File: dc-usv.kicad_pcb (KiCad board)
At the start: 4 copper layers, 160 x 100 mm, 310 parts, among them J1 Output 2.0mm, J2 Output 2.0mm, J3 Output 2.0mm, J5 HanRun_HR911105A, J6 USB_C_Receptacle_USB2.0, J7 Input 2.0mm, J8 Input 2.5mm, J9 USB_C_Receptacle_USB2.0, Q1 AON7544, Q10 AO4407A, Q11 2N7002, Q12 MMBT3904, Q13 2N7002, Q14 2N7002, Q15 2N7002, Q16 2N7002, Q17 2N7002, Q18 MMBT3904, Q19 AO4407A, Q2 AO3401A, Q20 2N7002, Q21 AO4407A, Q22 2N7002, Q23 AO4407A, Q24 2N7002, Q25 AO3401A, Q28 MMBT3904, Q29 MMBT3904, Q3 AON7544, Q30 MMBT3904, Q31 2N7002, Q32 AO4407A, Q33 MMBT3904, Q34 2N7002, Q35 AO4407A, Q36 MMBT3904, Q37 2N7002, Q38 AO4407A, Q4 AON7544, Q5 AON7544, Q6 CSD17308Q3, Q7 CSD17308Q3, Q8 AO4407A, Q9 2N7002, SW1 SW_DIP_x02, U1 BQ40z50-R2, U10 LAN8720A, U11 74HC595, U12 SY8105, U13 LM75B, U14 INA219AxD, U15 INA219AxD, U16 CH340G, U17 N066-6448TSWEG03-H28, U2 LM75B, U3 BQ24715, U4 TPS61178x, U5 INA219AxD, U6 INA219AxD, U7 LM75B, U8 SY8120B1ABC, U9 ESP32-WROOM-32E, Y1 12MHz

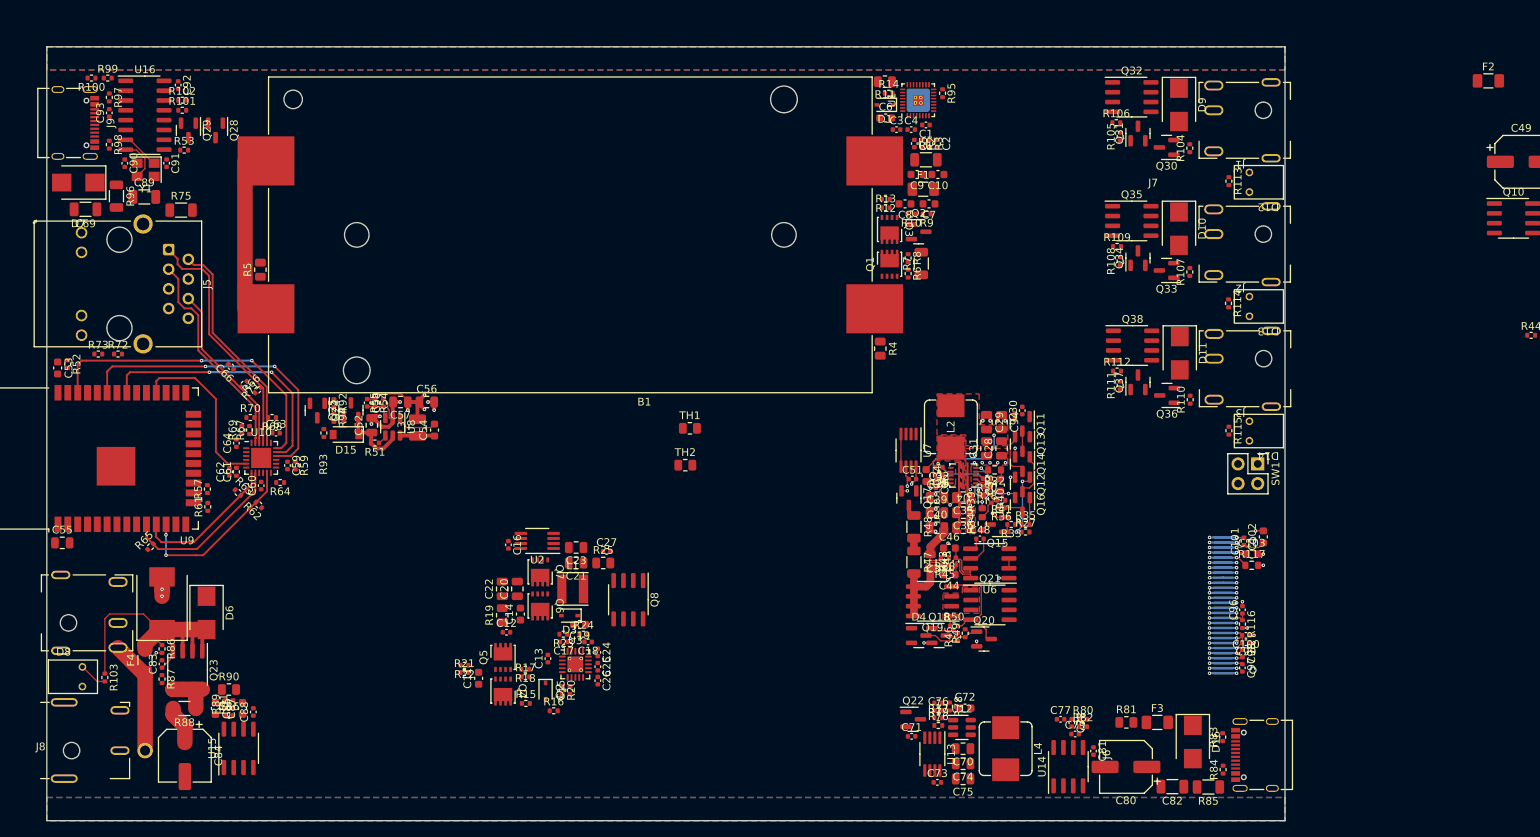
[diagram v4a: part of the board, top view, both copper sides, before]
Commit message: Plan front panel element positioning
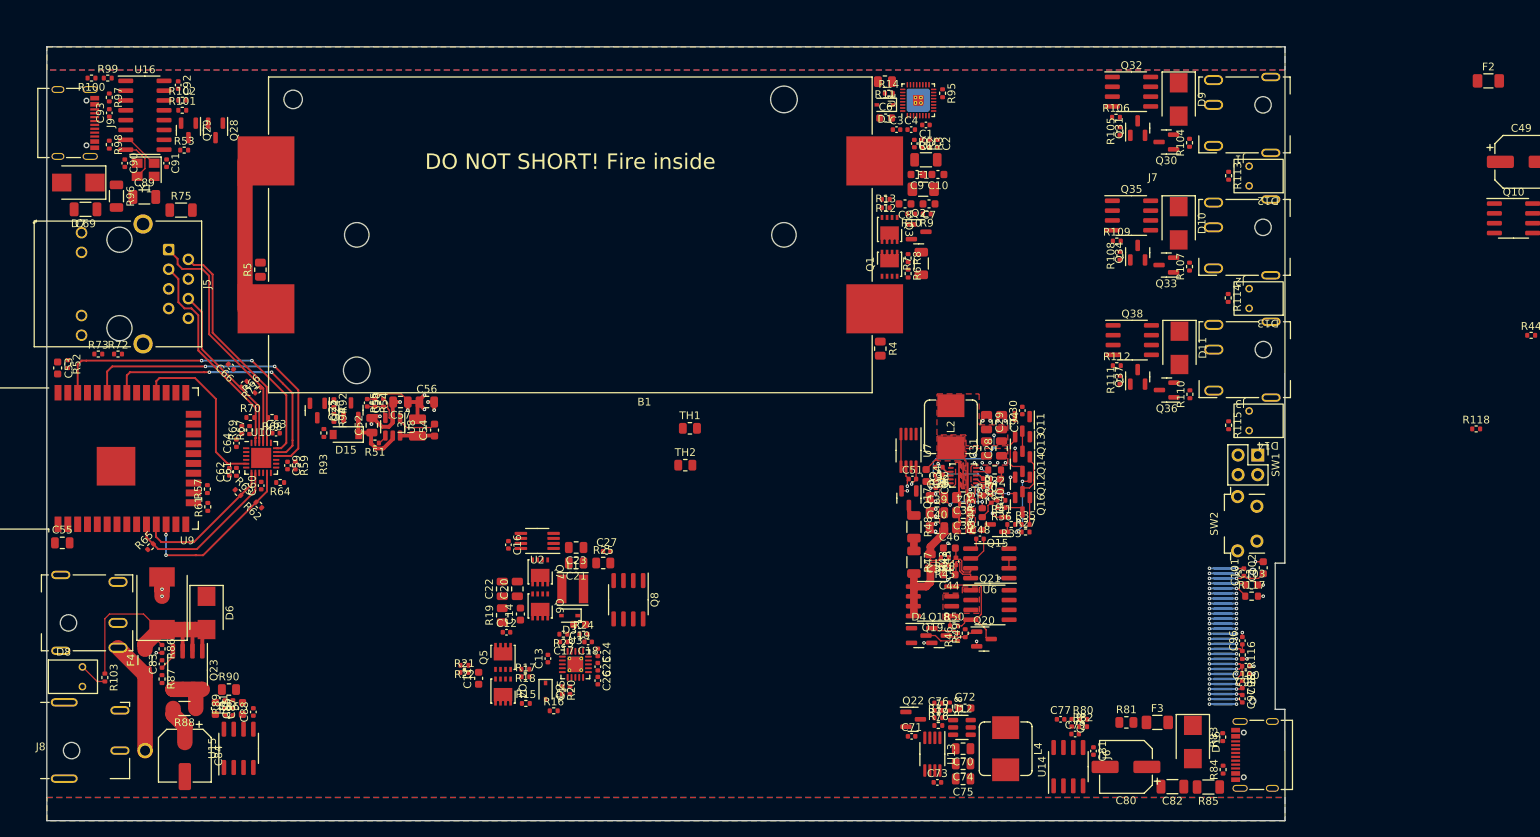
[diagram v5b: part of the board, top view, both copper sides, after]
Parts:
- added R118: 10k, Resistor_SMD:R_0402_1005Metric, F.Cu at (204.7, 69.4)
- added SW2: SW_Push, Button_Switch_SMD_LCSC:x-1825027-x, F.Cu at (176.4, 81.6)
- moved C100 3.99 mm to (174.9, 100.0)
- moved C103 3.99 mm to (175.7, 89.5)
- moved R116 3.99 mm to (174.5, 98.6)
- moved U17 3.99 mm to (173.8, 96.2)
- moved C101 3.99 mm to (174.7, 87.9)
- moved C102 3.99 mm to (177.2, 87.3)
- moved C96 3.99 mm to (174.5, 96.7)
- moved C97 3.99 mm to (174.5, 104.2)
- moved C98 3.99 mm to (174.5, 102.4)
- moved C99 3.99 mm to (174.9, 101.0)
- moved R117 3.99 mm to (175.7, 91.0)
- moved D14 1.33 mm to (179.8, 68.3)
- moved J3 1.18 mm to (181.2, 59.1)
- moved SW1 1.15 mm to (176.5, 72.8)
- moved D13 1.03 mm to (179.8, 52.5)
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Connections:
- U9 pad 5: unconnected-(U9-Pad5) -> /Control Logic/BUTTON
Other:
- outline, holes or cut-outs redrawn
- board text added: "DO NOT SHORT! Fire inside"

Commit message: Partial layout
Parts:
- added C104: 22nF, Capacitor_SMD:C_0402_1005Metric, F.Cu at (46.7, 104.3)
- added CASE1: 1455L1601, Case:1455L1601, F.Cu at (20.0, 20.0)
- added D17: YEL, LED_SMD:LED_0603_1608Metric, F.Cu at (50.3, 104.0)
- added D18: RED, LED_SMD:LED_0603_1608Metric, F.Cu at (50.3, 102.5)
- added D19: GRN, LED_SMD:LED_0603_1608Metric, F.Cu at (50.3, 105.6)
- added Q26: 2N7002, Package_TO_SOT_SMD:SOT-23, F.Cu at (54.2, 108.9)
- added R119: 10k, Resistor_SMD:R_0402_1005Metric, F.Cu at (48.3, 103.5)
- added R120: 5.1k, Resistor_SMD:R_0402_1005Metric, F.Cu at (52.8, 99.3)
- added R121: 10k, Resistor_SMD:R_0402_1005Metric, F.Cu at (48.3, 105.7)
- added U18: SRV05-4, Package_TO_SOT_SMD:SOT-23-6, F.Cu at (29.8, 29.9)
- TH1, TH2: footprint Resistor_SMD:R_0805_2012Metric -> Resistor_SMD:R_0402_1005Metric
- moved R56 136.3 mm to (134.9, 94.2)
- moved R31 130.0 mm to (112.2, 85.0)
- moved R95 99.6 mm to (92.3, 115.6), turned to 180 degrees
- moved C2 96.1 mm to (85.8, 115.0), turned to 180 degrees
- moved U1 95.0 mm to (91.4, 112.5), turned to 0 degrees
- moved C1 94.9 mm to (88.2, 113.5), turned to 90 degrees
- moved C10 94.9 mm to (81.8, 115.0), turned to 90 degrees
- moved R3 94.7 mm to (85.8, 114.0), turned to 180 degrees
- moved R2 93.3 mm to (85.8, 113.0), turned to 180 degrees
- moved R1 93.3 mm to (83.7, 113.5), turned to -90 degrees
- moved C7 92.5 mm to (78.0, 113.9), turned to 90 degrees
- moved C4 92.1 mm to (87.5, 111.6), turned to -90 degrees
- moved C5 92.0 mm to (85.8, 112.0), turned to 180 degrees
- moved F1 91.8 mm to (79.9, 113.1), turned to -90 degrees
- moved R9 91.8 mm to (76.7, 113.6), turned to 90 degrees
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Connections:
- net /Control Logic/ESP32 Debug/VBUS renamed VBUS
- net Net-(B1-Pad1) renamed /Battery Pack/B+
- net Net-(C11-Pad2) renamed /Charger/INFETCOM
- net Net-(C19-Pad2) renamed /Charger/LX
- net Net-(C72-Pad1) renamed /USB Output/LX
- net Net-(C74-Pad1) renamed /USB Output/VOUT
- net Net-(C8-Pad2) renamed /Battery Pack/VBAT
- net Net-(F3-Pad2) renamed /USB Output/VBUS
- net Net-(Q1-Pad5) renamed /Battery Pack/VCOM
- net Net-(Q23-Pad5) renamed /DC Input/DCSMOOTH
- C12 pad 2: /Charger/ACS- -> /Charger/ACS+
- C13 pad 1: /Charger/ACS- -> /Charger/ACS+
- C13 pad 2: /Charger/ACS+ -> /Charger/ACS-
- C14 pad 2: /Charger/ACS+ -> /Charger/ACS-
- C20 pad 1: /Charger/ACS+ -> /Charger/ACS-
- C22 pad 1: /Charger/ACS+ -> /Charger/ACS-
- C66 pad 1: +3.3V -> +3V3
- J5 pad 4: +3.3V -> +3V3
- J5 pad 5: +3.3V -> +3V3
- Q5 pad 5: /Charger/ACS- -> /Charger/ACS+
- Q5 pad 6: /Charger/ACS- -> /Charger/ACS+
- Q5 pad 7: /Charger/ACS- -> /Charger/ACS+
- Q5 pad 8: /Charger/ACS- -> /Charger/ACS+
- Q5 pad 9: /Charger/ACS- -> /Charger/ACS+
- Q6 pad 5: /Charger/ACS+ -> /Charger/ACS-
- Q6 pad 6: /Charger/ACS+ -> /Charger/ACS-
- Q6 pad 7: /Charger/ACS+ -> /Charger/ACS-
- Q6 pad 8: /Charger/ACS+ -> /Charger/ACS-
- Q6 pad 9: /Charger/ACS+ -> /Charger/ACS-
- R19 pad 1: /Charger/ACS- -> /Charger/ACS+
- R19 pad 2: /Charger/ACS+ -> /Charger/ACS-
- R66 pad 1: +3.3V -> +3V3
- R68 pad 1: +3.3V -> +3V3
- R70 pad 1: +3.3V -> +3V3
- R71 pad 1: +3.3V -> +3V3
- U3 pad 1: /Charger/ACS+ -> /Charger/ACS-
- U3 pad 2: /Charger/ACS- -> /Charger/ACS+
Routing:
- net SMBC: track 0.00 -> 222.1 mm, vias 0 -> 12
- net SMBD: track 1.26 -> 221.8 mm, vias 0 -> 12
- net SDA: track 7.65 -> 172.1 mm, vias 4 -> 12
- net SCL: track 3.50 -> 154.0 mm, vias 2 -> 10
- net VSEL1: track 0.93 -> 133.7 mm, vias 0 -> 4
- net GND: track 135.9 -> 266.8 mm, vias 77 -> 197
- net /Control Logic/~{OLED_RST}: track 5.22 -> 135.1 mm, vias 2 -> 5
- net /Control Logic/BUTTON: track 0.00 -> 118.6 mm, vias 0 -> 2
- net DCOK: track 0.00 -> 108.4 mm, vias 0 -> 5
- net /Charger/CS+: track 0.00 -> 103.9 mm, vias 0 -> 35
- net Net-(C3-Pad2): track 0.00 -> 94.4 mm
- net Net-(TH2-Pad2): track 0.00 -> 83.2 mm, vias 0 -> 4
- net Net-(TH1-Pad2): track 0.00 -> 65.0 mm, vias 0 -> 4
- net GND1: track 0.00 -> 64.5 mm, vias 0 -> 13
- net /Control Logic/EN: track 0.00 -> 61.5 mm, vias 0 -> 2
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- added copper zone on In2.Cu, net +3V3
- added copper zone on F.Cu, net /Battery Pack/B+
- added copper zone on In2.Cu, net /Battery Pack/BAT+
- added copper zone on F.Cu, net /Battery Pack/VBAT
- added copper zone on F.Cu, net /Battery Pack/VCOM
- added copper zone on F.Cu, net /Charger/ACS+
- added copper zone on F.Cu, net /Charger/ACS-
- added copper zone on B.Cu, net /Charger/CS+
- added copper zone on F.Cu, net /Charger/CS+
- added copper zone on In2.Cu, net /Charger/CS+
- added copper zone on F.Cu, net /Charger/CS-
- added copper zone on In2.Cu, net /Charger/CS-
- added copper zone on F.Cu, net /Charger/DCIN
- added copper zone on F.Cu, net /Charger/INFETCOM
- added copper zone on F.Cu, net /Charger/LX
- added copper zone on F.Cu, net /DC Input/DCSMOOTH
- added copper zone on F.Cu, net /USB Output/LX
- added copper zone on F.Cu, net /USB Output/VOUT
- added copper zone on In1.Cu, net GND
- added copper zone on F.Cu, net GND1
- added copper zone on In2.Cu, net GND1
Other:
- board size 160 x 100 mm -> 120 x 100 mm
- board text removed: "DO NOT SHORT! Fire inside"

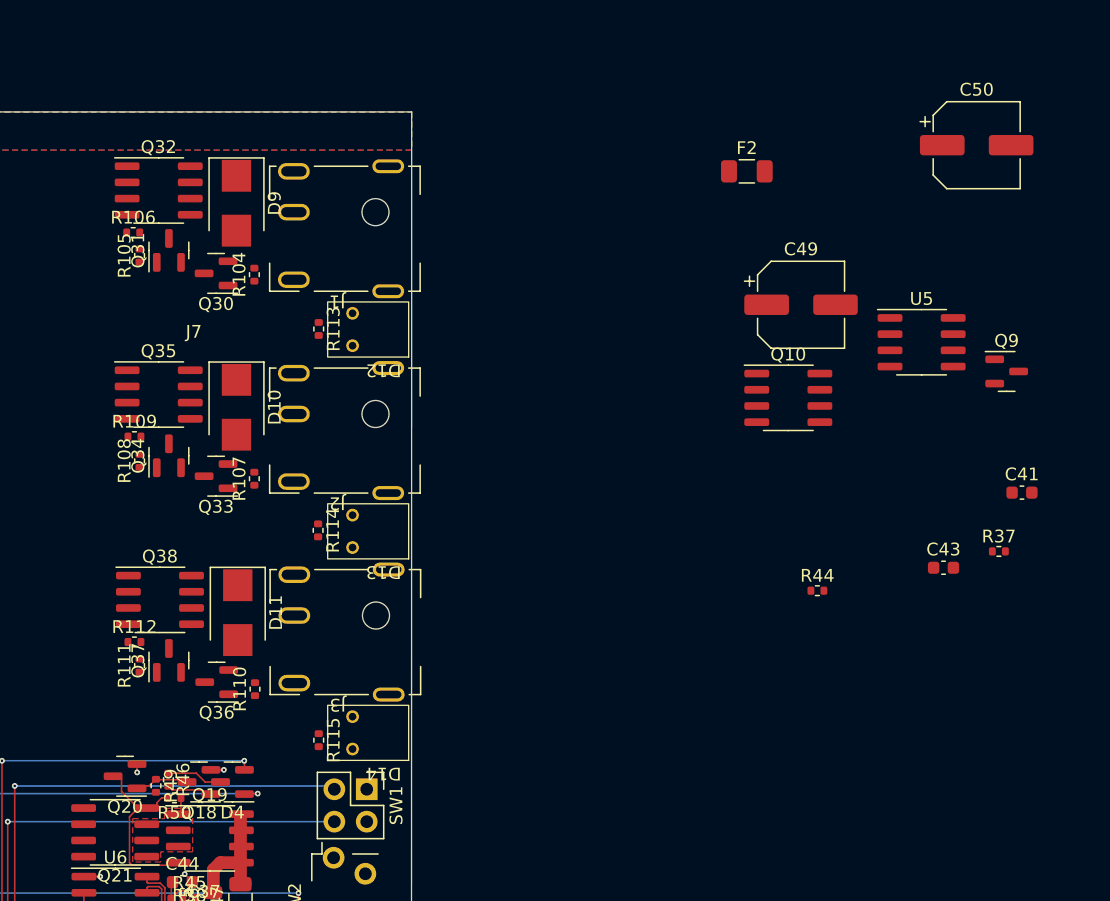
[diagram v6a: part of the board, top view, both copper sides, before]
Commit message: Partial DC out component placement
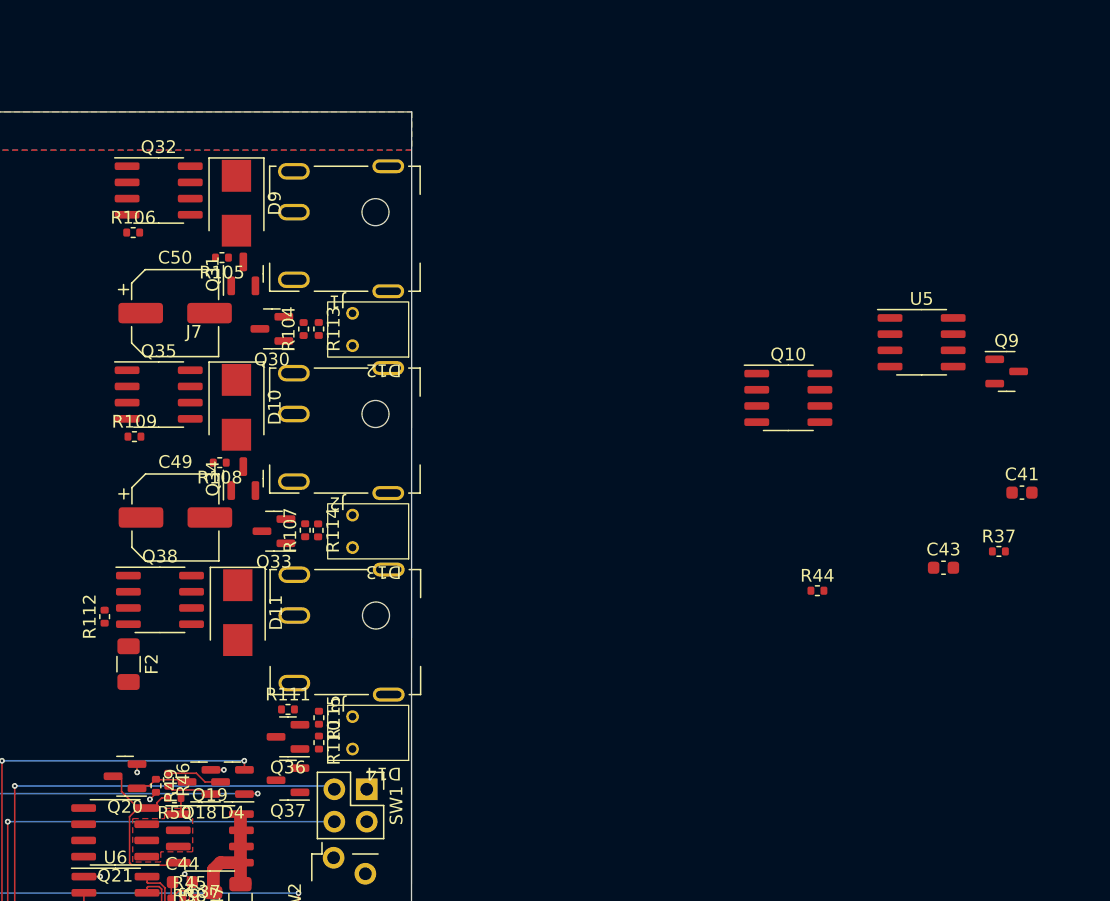
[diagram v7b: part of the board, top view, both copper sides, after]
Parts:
- moved C50 64.2 mm to (121.5, 35.8)
- moved F2 62.0 mm to (117.8, 63.3), turned to -90 degrees
- moved C49 51.8 mm to (121.5, 51.8)
- moved Q37 13.2 mm to (130.3, 72.4), turned to 180 degrees
- moved R111 12.1 mm to (130.3, 66.8), turned to 0 degrees
- moved Q36 7.04 mm to (130.3, 69.0)
- moved R110 6.53 mm to (132.7, 69.5), turned to -90 degrees
- moved R105 6.46 mm to (125.1, 31.4), turned to 180 degrees
- moved R108 6.29 mm to (125.0, 47.5), turned to 180 degrees
- moved Q33 6.26 mm to (129.2, 52.9)
- moved Q30 6.17 mm to (129.0, 37.0)
- moved Q31 6.12 mm to (126.8, 32.7)
- moved Q34 6.11 mm to (126.8, 48.8)
- moved R104 5.75 mm to (131.5, 37.0)
- moved R107 5.68 mm to (131.7, 52.8)
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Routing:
- net +3V3: track 73.0 -> 73.8 mm, vias 44 -> 45

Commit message: Finish initial layout
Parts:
- moved C47 107.5 mm to (122.3, 65.0), turned to -90 degrees
- moved C42 83.1 mm to (117.8, 62.0), turned to 180 degrees
- moved R42 82.7 mm to (123.0, 59.8), turned to 90 degrees
- moved R26 82.3 mm to (122.2, 68.6), turned to -90 degrees
- moved Q9 78.4 mm to (114.9, 72.1), turned to 180 degrees
- moved C41 68.3 mm to (120.6, 61.6)
- moved U5 67.3 mm to (119.1, 66.7), turned to 90 degrees
- moved R37 65.2 mm to (121.1, 60.3)
- moved C43 60.7 mm to (121.0, 57.3), turned to -90 degrees
- moved R44 50.7 mm to (121.1, 59.4)
- moved Q10 50.3 mm to (125.4, 66.7), turned to -90 degrees
- moved C68 28.2 mm to (114.9, 59.2)
- moved U11 28.0 mm to (116.5, 53.5)
- moved C65 28.0 mm to (112.2, 51.6)
- moved R74 28.0 mm to (112.2, 49.8)
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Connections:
- net Net-(F2-Pad2) renamed /DC Control/DCBUS
- net Net-(Q10-Pad1) renamed /DC Control/DCTHRU
- D4 pad 1: DC_OUT_OFF -> DCOK
- D4 pad 2: DCOK -> DC_OUT_OFF
- U11 pad 1: USB_OUT_OFF -> DC_OUT3_OFF
- U11 pad 15: DC_OUT_OFF -> unconnected-(U11-Pad15)
- U11 pad 3: DC_OUT1_OFF -> DC_OUT_OFF
- U11 pad 4: DC_OUT2_OFF -> USB_OUT_OFF
- U11 pad 5: DC_OUT3_OFF -> DC_OUT2_OFF
- U11 pad 6: unconnected-(U11-Pad6) -> DC_OUT1_OFF
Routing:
- net /Control Logic/GPIO_LATCH: track 0.00 -> 112.2 mm, vias 0 -> 2
- net /Control Logic/GPIO_CLK: track 0.00 -> 111.2 mm, vias 0 -> 2
- net /Control Logic/GPIO_DATA: track 0.00 -> 102.7 mm, vias 0 -> 2
- net DCOK: track 108.4 -> 195.2 mm, vias 5 -> 6
- net VSEL0: track 41.7 -> 123.9 mm, vias 1 -> 3
- net USB_OUT_OFF: track 3.57 -> 69.9 mm, vias 0 -> 2
- net GND: track 266.8 -> 328.9 mm, vias 197 -> 235
- net DC_OUT1_OFF: track 0.00 -> 39.1 mm, vias 0 -> 2
- net DC_OUT2_OFF: track 0.00 -> 32.5 mm, vias 0 -> 2
- net DC_OUT_TEST: track 30.2 -> 60.6 mm
- net DC_OUT3_OFF: track 0.00 -> 27.9 mm, vias 0 -> 2
- net Net-(D10-Pad1): track 0.00 -> 27.3 mm
- net Net-(Q36-Pad3): track 0.00 -> 25.8 mm
- net Net-(Q34-Pad3): track 0.00 -> 25.6 mm, vias 0 -> 2
- net Net-(D9-Pad1): track 0.00 -> 24.8 mm
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- added copper zone on B.Cu, net /Charger/DCIN
- added copper zone on In2.Cu, net /Charger/DCIN
- added copper zone on F.Cu, net /DC Control/DCBUS
- added copper zone on In2.Cu, net /DC Control/DCBUS
- added copper zone on F.Cu, net /DC Control/DCOUT
- added copper zone on F.Cu, net /DC Control/DCTHRU
